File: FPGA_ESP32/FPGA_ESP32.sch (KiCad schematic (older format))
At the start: 0 parts

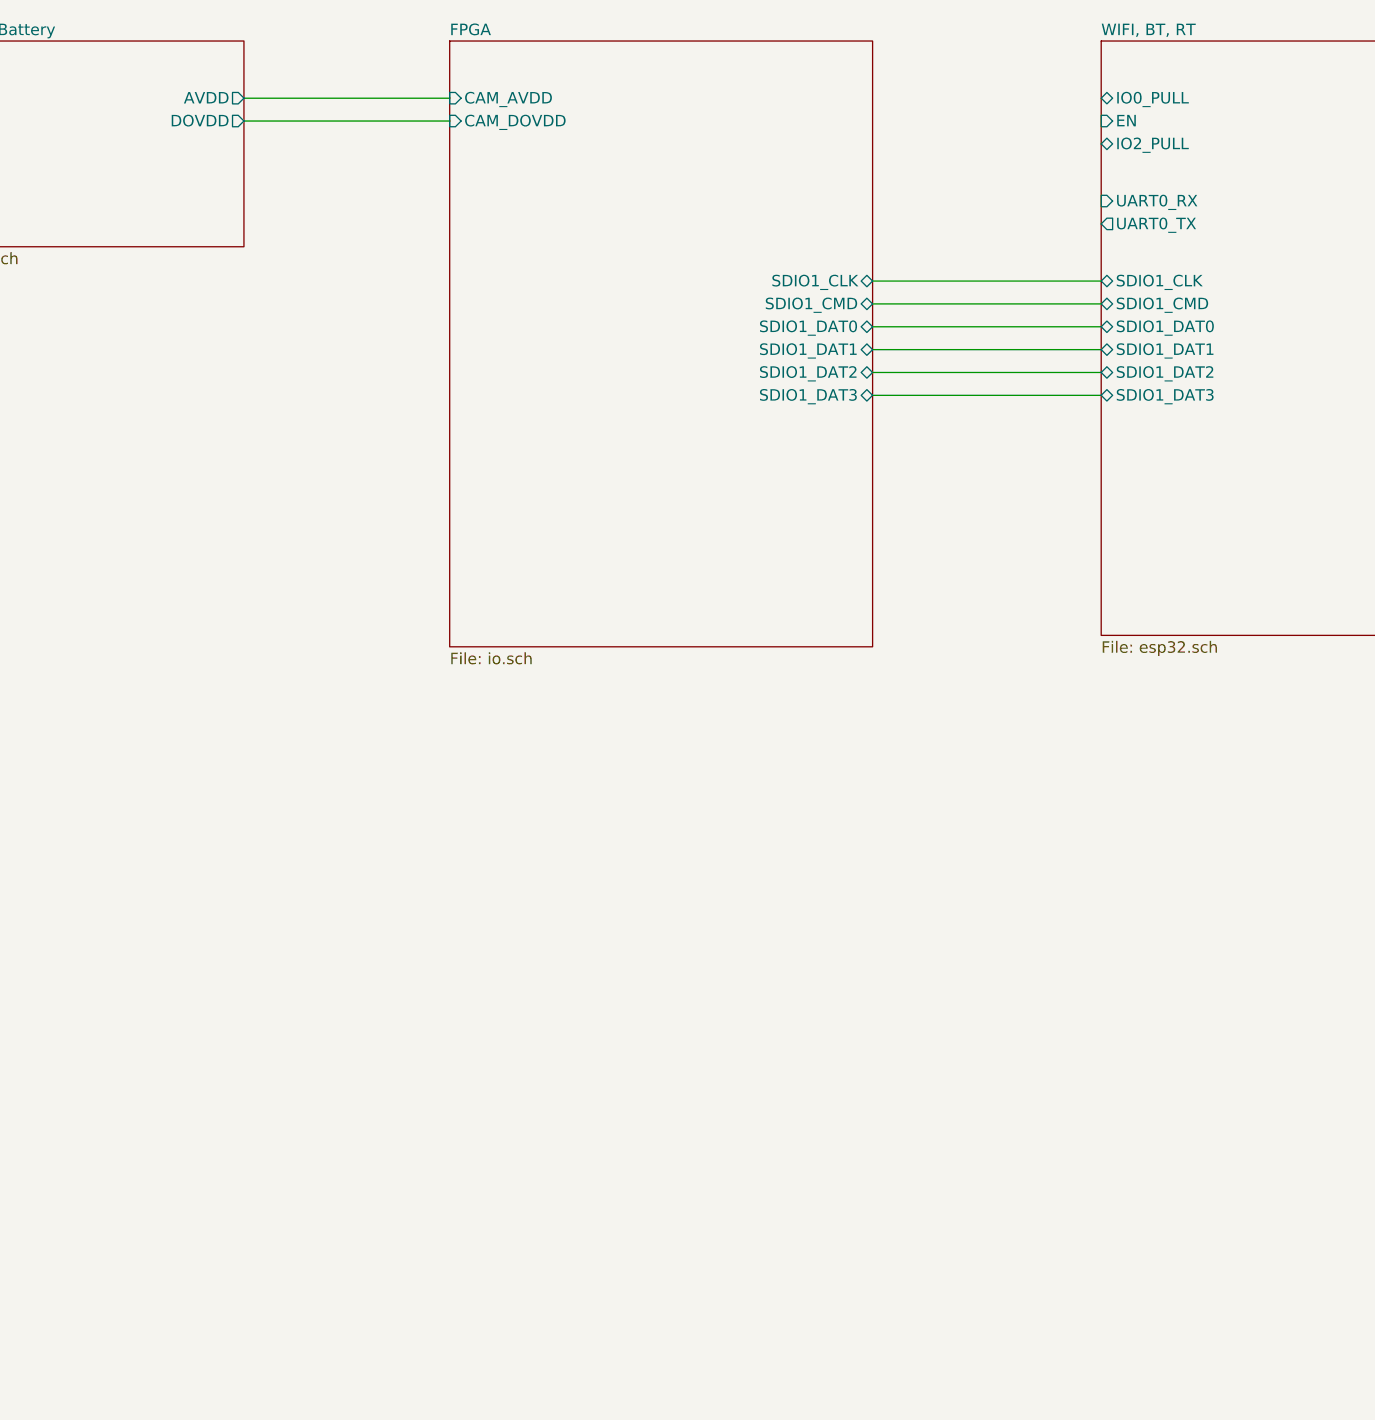
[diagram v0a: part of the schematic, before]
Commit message: FPGA_ESP32 : add header + esp32 with SDIO
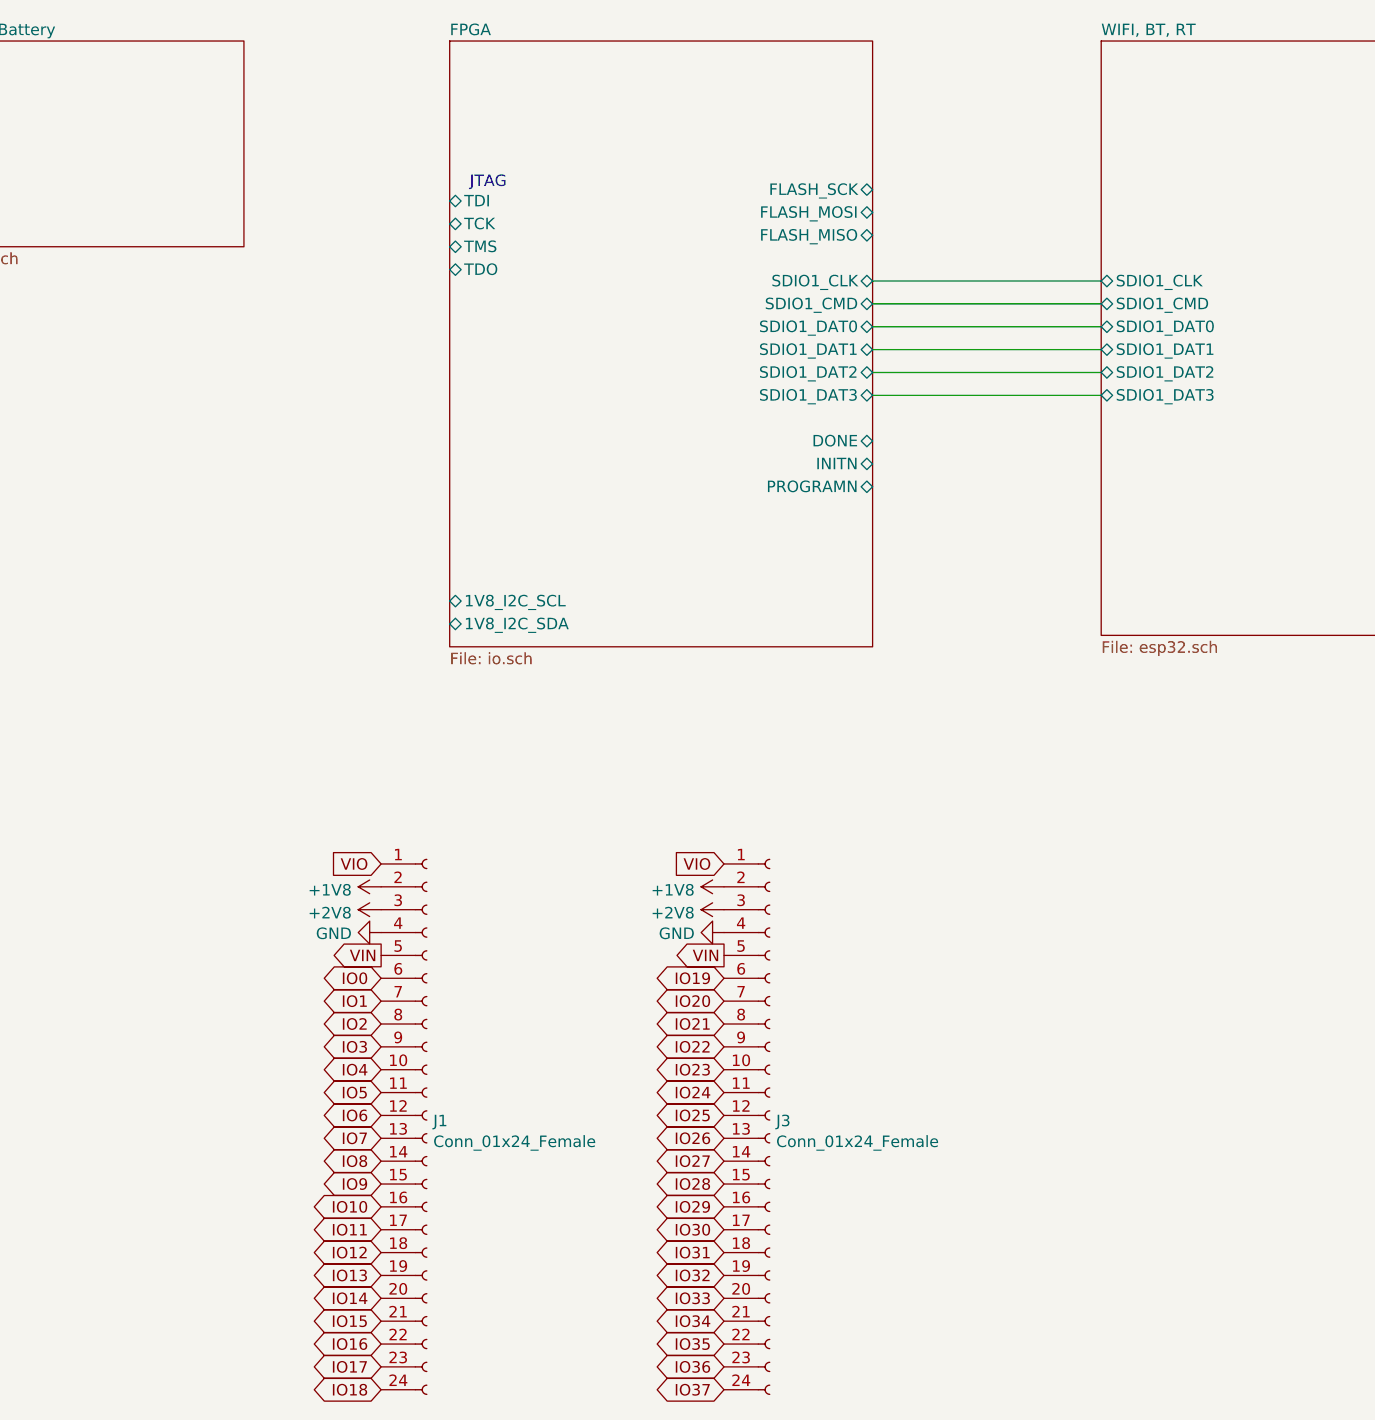
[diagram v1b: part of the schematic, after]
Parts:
- added J1, J3: Conn_01x24_Female, Connector_PinHeader_1.00mm:PinHeader_1x24_P1.00mm_Vertical, symbol Connector:Conn_01x24_Female
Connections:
- new net +1V8: J1.2 (Pin_2), J3.2 (Pin_2)
- new net +2V8: J1.3 (Pin_3), J3.3 (Pin_3)
- new net GND: J1.4 (Pin_4), J3.4 (Pin_4)
- new net IO0: J1.6 (Pin_6)
- new net IO1: J1.7 (Pin_7)
- new net IO10: J1.16 (Pin_16)
- new net IO11: J1.17 (Pin_17)
- new net IO12: J1.18 (Pin_18)
- new net IO13: J1.19 (Pin_19)
- new net IO14: J1.20 (Pin_20)
- new net IO15: J1.21 (Pin_21)
- new net IO16: J1.22 (Pin_22)
- new net IO17: J1.23 (Pin_23)
- new net IO18: J1.24 (Pin_24)
- new net IO19: J3.6 (Pin_6)
- new net IO2: J1.8 (Pin_8)
- new net IO20: J3.7 (Pin_7)
- new net IO21: J3.8 (Pin_8)
- new net IO22: J3.9 (Pin_9)
- new net IO23: J3.10 (Pin_10)
- new net IO24: J3.11 (Pin_11)
- new net IO25: J3.12 (Pin_12)
- new net IO26: J3.13 (Pin_13)
- new net IO27: J3.14 (Pin_14)
- new net IO28: J3.15 (Pin_15)
- new net IO29: J3.16 (Pin_16)
- new net IO3: J1.9 (Pin_9)
- new net IO30: J3.17 (Pin_17)
- new net IO31: J3.18 (Pin_18)
- new net IO32: J3.19 (Pin_19)
- new net IO33: J3.20 (Pin_20)
- new net IO34: J3.21 (Pin_21)
- new net IO35: J3.22 (Pin_22)
- new net IO36: J3.23 (Pin_23)
- new net IO37: J3.24 (Pin_24)
- new net IO4: J1.10 (Pin_10)
- new net IO5: J1.11 (Pin_11)
- new net IO6: J1.12 (Pin_12)
- new net IO7: J1.13 (Pin_13)
- new net IO8: J1.14 (Pin_14)
- new net IO9: J1.15 (Pin_15)
- new net VIN: J1.5 (Pin_5), J3.5 (Pin_5)
- new net VIO: J1.1 (Pin_1), J3.1 (Pin_1)
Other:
- note added: "JTAG"
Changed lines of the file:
@@
 F0 "PMIC Power Battery" 50
 F1 "power.sch" 50
-F2 "AVDD" O R 6350 3450 50
-F3 "DOVDD" O R 6350 3550 50
 $EndSheet
 Wire Wire Line
@@
 Wire Wire Line
 	10100 4750 9100 4750
-Wire Wire Line
-	6350 3450 7250 3450
-Wire Wire Line
-	7250 3550 6350 3550
 $Sheet
 S 10100 3200 2100 2600
@@
 F0 "WIFI, BT, RT" 50
 F1 "esp32.sch" 50
-F2 "EN" I L 10100 3550 50
-F3 "UART0_RX" I L 10100 3900 50
-F4 "UART0_TX" O L 10100 4000 50
-F5 "SDIO1_CLK" B L 10100 4250 50
-F6 "SDIO1_CMD" B L 10100 4350 50
-F7 "SDIO1_DAT1" B L 10100 4550 50
-F8 "SDIO1_DAT2" B L 10100 4650 50
-F9 "SDIO1_DAT3" B L 10100 4750 50
-F10 "IO2_PULL" B L 10100 3650 50
-F11 "SDIO1_DAT0" B L 10100 4450 50
-F12 "IO0_PULL" B L 10100 3450 50
-F13 "SD2" B R 12200 4800 50
-F14 "SD3" B R 12200 5000 50
+F2 "SDIO1_CLK" B L 10100 4250 50
+F3 "SDIO1_CMD" B L 10100 4350 50
+F4 "SDIO1_DAT1" B L 10100 4550 50
+F5 "SDIO1_DAT2" B L 10100 4650 50
+F6 "SDIO1_DAT3" B L 10100 4750 50
+F7 "SDIO1_DAT0" B L 10100 4450 50
+F8 "SD2" B R 12200 4800 50
+F9 "SD3" B R 12200 5000 50
 $EndSheet
 NoConn ~ 12200 5000
@@
 F6 "SDIO1_DAT3" B R 9100 4750 50
 F7 "SDIO1_DAT0" B R 9100 4450 50
-F8 "CAM_AVDD" I L 7250 3450 50
-F9 "CAM_DOVDD" I L 7250 3550 50
+F8 "TDI" B L 7250 3900 50
+F9 "TCK" B L 7250 4000 50
+F10 "TMS" B L 7250 4100 50
+F11 "TDO" B L 7250 4200 50
+F12 "FLASH_MISO" B R 9100 4050 50
+F13 "FLASH_MOSI" B R 9100 3950 50
+F14 "FLASH_SCK" B R 9100 3850 50
+F15 "DONE" B R 9100 4950 50
+F16 "INITN" B R 9100 5050 50
+F17 "PROGRAMN" B R 9100 5150 50
+F18 "1V8_I2C_SDA" B L 7250 5750 50
+F19 "1V8_I2C_SCL" B L 7250 5650 50
 $EndSheet
+$Comp
+L Connector:Conn_01x24_Female J1
+U 1 1 5EF79A02
+P 7150 7900
+F 0 "J1" H 7178 7876 50  0000 L CNN
+F 1 "Conn_01x24_Female" H 7178 7785 50  0000 L CNN
+F 2 "Connector_PinHeader_1.00mm:PinHeader_1x24_P1.00mm_Vertical" H 7150 7900 50  0001 C CNN
+F 3 "~" H 7150 7900 50  0001 C CNN
+	1    7150 7900
+	1    0    0    -1
+$EndComp
+$Comp
+L Connector:Conn_01x24_Female J3
+U 1 1 5EF7DB79
+P 8650 7900
+F 0 "J3" H 8678 7876 50  0000 L CNN
+F 1 "Conn_01x24_Female" H 8678 7785 50  0000 L CNN
+F 2 "Connector_PinHeader_1.00mm:PinHeader_1x24_P1.00mm_Vertical" H 8650 7900 50  0001 C CNN
+F 3 "~" H 8650 7900 50  0001 C CNN
+	1    8650 7900
+	1    0    0    -1
+$EndComp
+Text Notes 7500 3850 2    50   ~ 0
+JTAG
+Text GLabel 6950 6800 0    50   Input ~ 0
+VIO
+$Comp
+L power:+1V8 #PWR?
+U 1 1 5F1F5F39
+P 6950 6900
+AR Path="/5BC231CE/5F1F5F39" Ref="#PWR?"  Part="1"
+AR Path="/5BC231CB/5F1F5F39" Ref="#PWR?"  Part="1"
+AR Path="/5F1F5F39" Ref="#PWR?"  Part="1"
+F 0 "#PWR?" H 6950 6750 50  0001 C CNN
+F 1 "+1V8" V 6965 7028 50  0000 L CNN
+F 2 "" H 6950 6900 50  0001 C CNN
+F 3 "" H 6950 6900 50  0001 C CNN
+	1    6950 6900
+	0    -1   1    0
+$EndComp
+$Comp
+L power:+2V8 #PWR?
+U 1 1 5F1F5F3F
+P 6950 7000
+AR Path="/5BC231CE/5F1F5F3F" Ref="#PWR?"  Part="1"
+AR Path="/5BC231CB/5F1F5F3F" Ref="#PWR?"  Part="1"
+AR Path="/5F1F5F3F" Ref="#PWR?"  Part="1"
+F 0 "#PWR?" H 6950 6850 50  0001 C CNN
+F 1 "+2V8" V 6965 7128 50  0000 L CNN
+F 2 "" H 6950 7000 50  0001 C CNN
+F 3 "" H 6950 7000 50  0001 C CNN
+	1    6950 7000
+	0    -1   1    0
+$EndComp
+$Comp
+L power:GND #PWR?
+U 1 1 5F1F73BB
+P 6950 7100
+F 0 "#PWR?" H 6950 6850 50  0001 C CNN
+F 1 "GND" V 6955 6972 50  0000 R CNN
+F 2 "" H 6950 7100 50  0001 C CNN
+F 3 "" H 6950 7100 50  0001 C CNN
+	1    6950 7100
+	0    1    1    0
+$EndComp
+Text GLabel 6950 7300 0    50   BiDi ~ 0
+IO0
+Text GLabel 6950 7400 0    50   BiDi ~ 0
+IO1
+Text GLabel 6950 7500 0    50   BiDi ~ 0
+IO2
+Text GLabel 6950 7600 0    50   BiDi ~ 0
+IO3
+Text GLabel 6950 7700 0    50   BiDi ~ 0
+IO4
+Text GLabel 6950 7800 0    50   BiDi ~ 0
+IO5
+Text GLabel 6950 7900 0    50   BiDi ~ 0
+IO6
+Text GLabel 6950 8000 0    50   BiDi ~ 0
+IO7
+Text GLabel 6950 8100 0    50   BiDi ~ 0
+IO8
+Text GLabel 6950 8200 0    50   BiDi ~ 0
+IO9
+Text GLabel 6950 8300 0    50   BiDi ~ 0
+IO10
+Text GLabel 6950 8400 0    50   BiDi ~ 0
+IO11
+Text GLabel 6950 8500 0    50   BiDi ~ 0
+IO12
+Text GLabel 6950 8600 0    50   BiDi ~ 0
+IO13
+Text GLabel 6950 8700 0    50   BiDi ~ 0
+IO14
+Text GLabel 6950 8800 0    50   BiDi ~ 0
+IO15
+Text GLabel 6950 8900 0    50   BiDi ~ 0
+IO16
+Text GLabel 6950 9000 0    50   BiDi ~ 0
+IO17
+Text GLabel 6950 9100 0    50   BiDi ~ 0
+IO18
+Text GLabel 8450 7300 0    50   BiDi ~ 0
+IO19
+Text GLabel 8450 7400 0    50   BiDi ~ 0
+IO20
+Text GLabel 8450 7500 0    50   BiDi ~ 0
+IO21
+Text GLabel 8450 6800 0    50   Input ~ 0
+VIO
+$Comp
+L power:+1V8 #PWR?
+U 1 1 5F20AE65
+P 8450 6900
+AR Path="/5BC231CE/5F20AE65" Ref="#PWR?"  Part="1"
+AR Path="/5BC231CB/5F20AE65" Ref="#PWR?"  Part="1"
+AR Path="/5F20AE65" Ref="#PWR?"  Part="1"
+F 0 "#PWR?" H 8450 6750 50  0001 C CNN
+F 1 "+1V8" V 8465 7028 50  0000 L CNN
+F 2 "" H 8450 6900 50  0001 C CNN
+F 3 "" H 8450 6900 50  0001 C CNN
+	1    8450 6900
+	0    -1   1    0
+$EndComp
+$Comp
+L power:+2V8 #PWR?
+U 1 1 5F20AE6B
+P 8450 7000
+AR Path="/5BC231CE/5F20AE6B" Ref="#PWR?"  Part="1"
+AR Path="/5BC231CB/5F20AE6B" Ref="#PWR?"  Part="1"
+AR Path="/5F20AE6B" Ref="#PWR?"  Part="1"
+F 0 "#PWR?" H 8450 6850 50  0001 C CNN
+F 1 "+2V8" V 8465 7128 50  0000 L CNN
+F 2 "" H 8450 7000 50  0001 C CNN
+F 3 "" H 8450 7000 50  0001 C CNN
+	1    8450 7000
+	0    -1   1    0
+$EndComp
+$Comp
+L power:GND #PWR?
+U 1 1 5F20AE71
+P 8450 7100
+F 0 "#PWR?" H 8450 6850 50  0001 C CNN
+F 1 "GND" V 8455 6972 50  0000 R CNN
+F 2 "" H 8450 7100 50  0001 C CNN
+F 3 "" H 8450 7100 50  0001 C CNN
+	1    8450 7100
+	0    1    1    0
+$EndComp
+Text GLabel 8450 7600 0    50   BiDi ~ 0
+IO22
+Text GLabel 8450 7700 0    50   BiDi ~ 0
+IO23
+Text GLabel 8450 7800 0    50   BiDi ~ 0
+IO24
+Text GLabel 8450 7900 0    50   BiDi ~ 0
+IO25
+Text GLabel 8450 8000 0    50   BiDi ~ 0
+IO26
+Text GLabel 8450 8100 0    50   BiDi ~ 0
+IO27
+Text GLabel 8450 8200 0    50   BiDi ~ 0
+IO28
+Text GLabel 8450 8300 0    50   BiDi ~ 0
+IO29
+Text GLabel 8450 8400 0    50   BiDi ~ 0
+IO30
+Text GLabel 8450 8500 0    50   BiDi ~ 0
+IO31
+Text GLabel 8450 8600 0    50   BiDi ~ 0
+IO32
+Text GLabel 8450 8700 0    50   BiDi ~ 0
+IO33
+Text GLabel 8450 8800 0    50   BiDi ~ 0
+IO34
+Text GLabel 8450 8900 0    50   BiDi ~ 0
+IO35
+Text GLabel 8450 9000 0    50   BiDi ~ 0
+IO36
+Text GLabel 8450 9100 0    50   BiDi ~ 0
+IO37
+Text GLabel 6950 7200 0    50   Output ~ 0
+VIN
+Text GLabel 8450 7200 0    50   Output ~ 0
+VIN
 $EndSCHEMATC

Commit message: FPGA_ESP32 : add 2 psram ic, rf switch
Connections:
- no-connect marks 2 -> 0
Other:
- note removed: "JTAG"
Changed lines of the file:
@@
 F6 "SDIO1_DAT3" B L 10100 4750 50
 F7 "SDIO1_DAT0" B L 10100 4450 50
-F8 "SD2" B R 12200 4800 50
-F9 "SD3" B R 12200 5000 50
+F8 "FPGA_DONE" B L 10100 4950 50
+F9 "FPGA_PROGRAMN" B L 10100 5150 50
+F10 "INITN" B L 10100 5050 50
+F11 "FLASH_MISO" B L 10100 4050 50
+F12 "FLASH_MOSI" B L 10100 3950 50
+F13 "FLASH_CLK" B L 10100 3850 50
 $EndSheet
-NoConn ~ 12200 5000
-NoConn ~ 12200 4800
 $Sheet
 S 7250 3200 1850 2650
@@
 F6 "SDIO1_DAT3" B R 9100 4750 50
 F7 "SDIO1_DAT0" B R 9100 4450 50
-F8 "TDI" B L 7250 3900 50
-F9 "TCK" B L 7250 4000 50
-F10 "TMS" B L 7250 4100 50
-F11 "TDO" B L 7250 4200 50
-F12 "FLASH_MISO" B R 9100 4050 50
-F13 "FLASH_MOSI" B R 9100 3950 50
-F14 "FLASH_SCK" B R 9100 3850 50
-F15 "DONE" B R 9100 4950 50
-F16 "INITN" B R 9100 5050 50
-F17 "PROGRAMN" B R 9100 5150 50
-F18 "1V8_I2C_SDA" B L 7250 5750 50
-F19 "1V8_I2C_SCL" B L 7250 5650 50
+F8 "FLASH_MISO" B R 9100 4050 50
+F9 "FLASH_MOSI" B R 9100 3950 50
+F10 "FLASH_SCK" B R 9100 3850 50
+F11 "DONE" B R 9100 4950 50
+F12 "INITN" B R 9100 5050 50
+F13 "PROGRAMN" B R 9100 5150 50
+F14 "1V8_I2C_SDA" B L 7250 5750 50
+F15 "1V8_I2C_SCL" B L 7250 5650 50
 $EndSheet
 $Comp
@@
 	1    0    0    -1
 $EndComp
-Text Notes 7500 3850 2    50   ~ 0
-JTAG
 Text GLabel 6950 6800 0    50   Input ~ 0
 VIO
@@
 AR Path="/5BC231CE/5F1F5F39" Ref="#PWR?"  Part="1"
 AR Path="/5BC231CB/5F1F5F39" Ref="#PWR?"  Part="1"
-AR Path="/5F1F5F39" Ref="#PWR?"  Part="1"
-F 0 "#PWR?" H 6950 6750 50  0001 C CNN
+AR Path="/5F1F5F39" Ref="#PWR0107"  Part="1"
+F 0 "#PWR0107" H 6950 6750 50  0001 C CNN
 F 1 "+1V8" V 6965 7028 50  0000 L CNN
 F 2 "" H 6950 6900 50  0001 C CNN
@@
 AR Path="/5BC231CE/5F1F5F3F" Ref="#PWR?"  Part="1"
 AR Path="/5BC231CB/5F1F5F3F" Ref="#PWR?"  Part="1"
-AR Path="/5F1F5F3F" Ref="#PWR?"  Part="1"
-F 0 "#PWR?" H 6950 6850 50  0001 C CNN
+AR Path="/5F1F5F3F" Ref="#PWR0108"  Part="1"
+F 0 "#PWR0108" H 6950 6850 50  0001 C CNN
 F 1 "+2V8" V 6965 7128 50  0000 L CNN
 F 2 "" H 6950 7000 50  0001 C CNN
@@
 $EndComp
 $Comp
-L power:GND #PWR?
+L power:GND #PWR0114
 U 1 1 5F1F73BB
 P 6950 7100
-F 0 "#PWR?" H 6950 6850 50  0001 C CNN
+F 0 "#PWR0114" H 6950 6850 50  0001 C CNN
 F 1 "GND" V 6955 6972 50  0000 R CNN
 F 2 "" H 6950 7100 50  0001 C CNN
@@
 AR Path="/5BC231CE/5F20AE65" Ref="#PWR?"  Part="1"
 AR Path="/5BC231CB/5F20AE65" Ref="#PWR?"  Part="1"
-AR Path="/5F20AE65" Ref="#PWR?"  Part="1"
-F 0 "#PWR?" H 8450 6750 50  0001 C CNN
+AR Path="/5F20AE65" Ref="#PWR0115"  Part="1"
+F 0 "#PWR0115" H 8450 6750 50  0001 C CNN
 F 1 "+1V8" V 8465 7028 50  0000 L CNN
 F 2 "" H 8450 6900 50  0001 C CNN
@@
 AR Path="/5BC231CE/5F20AE6B" Ref="#PWR?"  Part="1"
 AR Path="/5BC231CB/5F20AE6B" Ref="#PWR?"  Part="1"
-AR Path="/5F20AE6B" Ref="#PWR?"  Part="1"
-F 0 "#PWR?" H 8450 6850 50  0001 C CNN
+AR Path="/5F20AE6B" Ref="#PWR0116"  Part="1"
+F 0 "#PWR0116" H 8450 6850 50  0001 C CNN
 F 1 "+2V8" V 8465 7128 50  0000 L CNN
 F 2 "" H 8450 7000 50  0001 C CNN
@@
 $EndComp
 $Comp
-L power:GND #PWR?
+L power:GND #PWR0117
 U 1 1 5F20AE71
 P 8450 7100
-F 0 "#PWR?" H 8450 6850 50  0001 C CNN
+F 0 "#PWR0117" H 8450 6850 50  0001 C CNN
 F 1 "GND" V 8455 6972 50  0000 R CNN
 F 2 "" H 8450 7100 50  0001 C CNN
@@
 Text GLabel 8450 7200 0    50   Output ~ 0
 VIN
+Wire Wire Line
+	9100 4950 10100 4950
+Wire Wire Line
+	10100 5050 9100 5050
+Wire Wire Line
+	9100 5150 10100 5150
+Wire Wire Line
+	9100 3850 10100 3850
+Wire Wire Line
+	10100 3950 9100 3950
+Wire Wire Line
+	9100 4050 10100 4050
 $EndSCHEMATC

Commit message: FPGA_ESP32 : add camera, change header position
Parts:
- removed J1, J3: Conn_01x24_Female, Connector_PinHeader_1.00mm:PinHeader_1x24_P1.00mm_Vertical, symbol Connector:Conn_01x24_Female
- added H1, H2, H3: MountingHole_Pad, MountingHole:MountingHole_2.2mm_M2_Pad_Via, symbol Mechanical:MountingHole_Pad
- added H4: MountingHole_Pad, MountingHole:MountingHole_2.2mm_M2_Pad, symbol Mechanical:MountingHole_Pad
- added J1, J3, J4: Conn_01x18_Female, Connector_PinHeader_1.00mm:PinHeader_1x18_P1.00mm_Vertical, symbol Connector:Conn_01x18_Female
- added U1: LFE5UM-25F-7MG285C, footprints:BGA285N50P18X18_1000X1000X130N, symbol LFE5UM-25F-7MG285C:LFE5UM-25F-7MG285C
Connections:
- net labels added: +1V1, +2V5, EN, IO38, IO39, IO40
- net labels removed: VIN
- wire segments 12 -> 20
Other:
- note added: "1V1 Reg"
- note added: "1V8 Reg"
- note added: "2V5 Reg"
- note added: "2V8 Reg\nTODO : Check if 2V5 is enought for OV5640"
- note added: "3V3 Reg"

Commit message: FPGA_ESP32 : lot of fix + modification
Replace digital camera by analog camera decoder
Fix PSRAM io domain 3.3V -> 1.8V
Start reducing capacitor number
Add remaining psram pin
Sheet resize
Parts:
- removed J1, J3, J4: Conn_01x18_Female, Connector_PinHeader_1.00mm:PinHeader_1x18_P1.00mm_Vertical, symbol Connector:Conn_01x18_Female
- added J1, J3, J4, J5: Conn_01x14_Female, Connector_PinHeader_1.00mm:PinHeader_1x14_P1.00mm_Vertical, symbol Connector:Conn_01x14_Female
- added R1, R2, R3, R4: 4K7, Resistor_SMD:R_0201_0603Metric, symbol Device:R
- added unit 5 of U1
- H4: footprint MountingHole:MountingHole_2.2mm_M2_Pad -> MountingHole:MountingHole_2.2mm_M2_Pad_Via
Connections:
- net labels added: AVIN1, AVIN2, IO41
- net labels removed: +2V8, IO27
- wire segments 20 -> 28
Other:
- note removed: "2V8 Reg\nTODO : Check if 2V5 is enought for OV5640"
- moved on the sheet: H1, H2, H3, H4, U1J
